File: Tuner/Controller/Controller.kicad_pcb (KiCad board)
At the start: 2 copper layers, 100 x 100 mm, 180 parts, among them J1 Conn_02x05_Odd_Even, J10 Conn_01x05, J11 Conn_Coaxial, J13 Conn_Coaxial, J15 Conn_01x02, J16 Conn_01x08, J18 Conn_01x01, J19 Conn_01x01, J2 Conn_02x05_Odd_Even, J20 Conn_01x01, J21 Conn_01x01, J3 Conn_02x05_Odd_Even, J4 Conn_02x05_Odd_Even, J5 Conn_02x05_Odd_Even, J6 Conn_01x02, J7 Conn_02x05_Odd_Even, J8 Conn_01x06, J9 Conn_Coaxial, Q1 2N3904, Q10 2N7000, Q11 2N7000, Q12 2N7000, Q2 2N3904, Q3 2N3904, Q4 2N3904, Q5 2N3904, Q6 2N3904, Q7 2N3904, Q8 2N3904, Q9 2N7000, U1 74LS393, U2 74HC14, U3 74HC86, U4 LM350_TO220

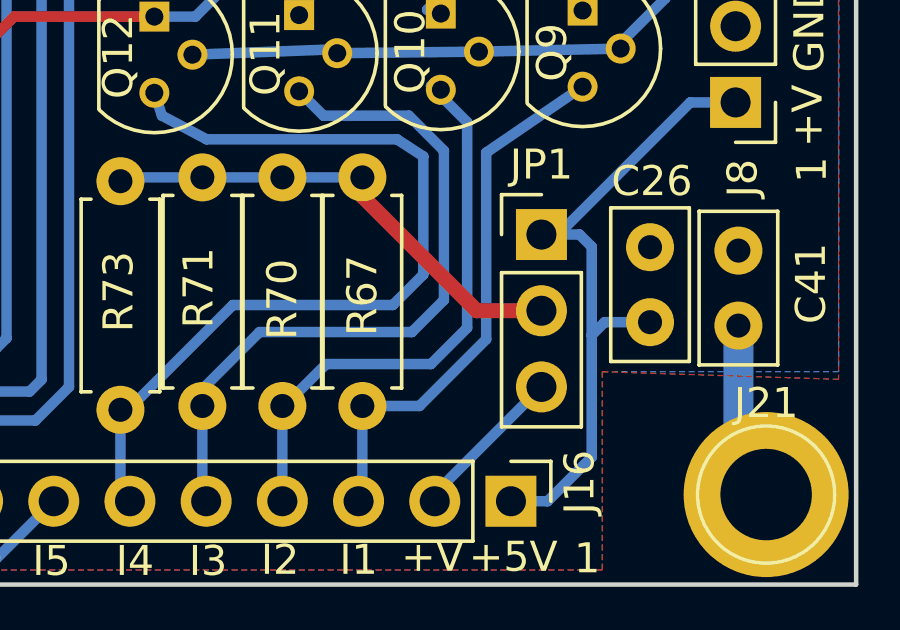
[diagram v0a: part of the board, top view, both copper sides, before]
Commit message: Added some initial I2C user interface stuff
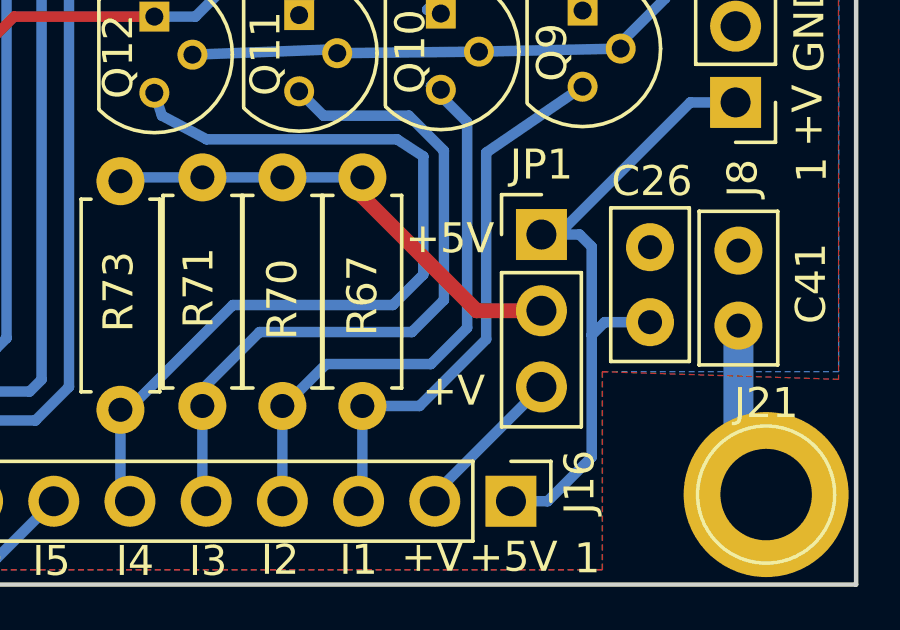
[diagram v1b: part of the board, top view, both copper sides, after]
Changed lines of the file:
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@@
     (links 401)
     (no_connects 0)
-    (area 52.252381 23.9975 155.74762 130.223619)
+    (area 53.924999 27.924999 154.075001 128.075001)
     (thickness 1.6)
-    (drawings 55)
+    (drawings 57)
     (tracks 1681)
     (zones 0)
@@
   )
   (setup
-    (last_trace_width 0.35)
+    (last_trace_width 0.25)
     (user_trace_width 0.35)
     (user_trace_width 0.5)
@@
     )
   )
+  (gr_text +5V (at 140.462 116.459) (layer F.SilkS)
+    (effects (font (size 1 1) (thickness 0.15)))
+  )
+  (gr_text +V (at 140.589 121.539) (layer F.SilkS)
+    (effects (font (size 1 1) (thickness 0.15)))
+  )
   (gr_text 1 (at 147.48764 41.95064 90) (layer F.SilkS)

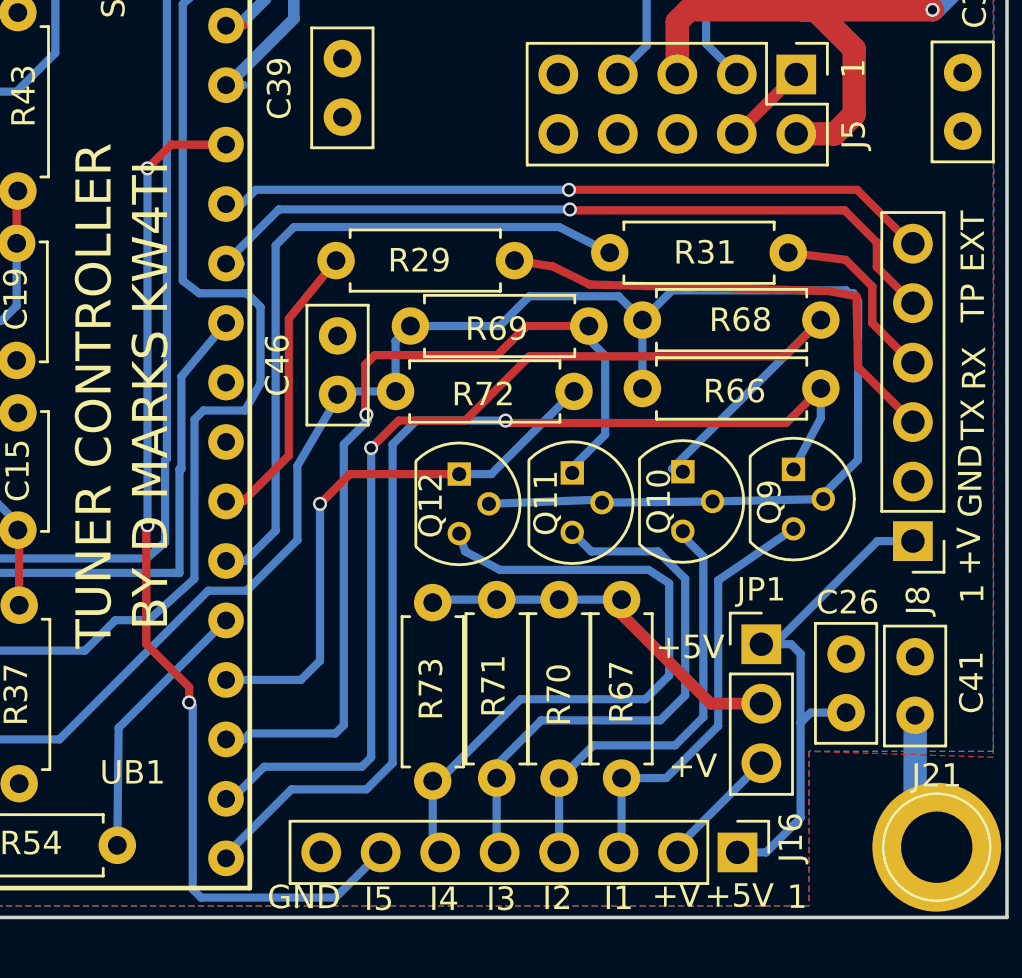
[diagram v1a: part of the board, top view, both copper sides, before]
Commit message: Moved digital signal interface connector over
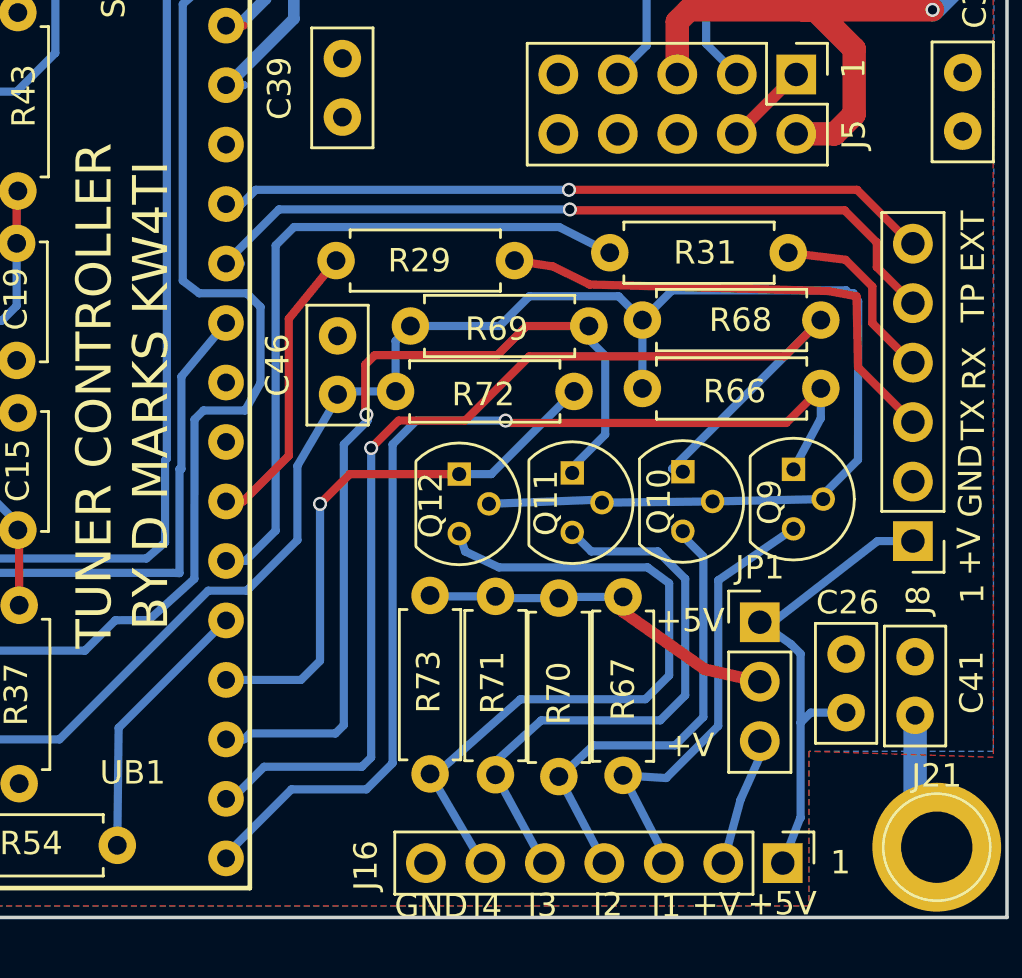
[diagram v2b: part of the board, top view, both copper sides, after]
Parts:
- J16: value Conn_01x08 -> Conn_01x07; footprint Pin_Headers:Pin_Header_Straight_1x08_Pitch2.54mm -> Pin_Headers:Pin_Header_Straight_1x07_Pitch2.54mm
- moved J16 1.98 mm to (144.4, 125.7)
- moved JP1 0.94 mm to (143.4, 115.4)
- moved R73 0.33 mm to (129.4, 121.9)
- moved R71 0.15 mm to (132.2, 121.9)
- moved R67 0.13 mm to (137.6, 121.9)
- moved R70 0.06 mm to (134.9, 122.0)
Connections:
- J16 pad 7: IO5 -> GND
- UB1 pad 41: IO5 -> (no net)
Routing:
- net IO5: track 44.4 -> 0.00 mm, vias 3 -> 0
- net +5V: track 134.2 -> 132.8 mm
- net Net-(J16-Pad6): track 29.0 -> 30.2 mm
- net Net-(J16-Pad5): track 24.3 -> 25.3 mm
- net Net-(J16-Pad4): track 19.6 -> 20.6 mm
- net Net-(J16-Pad3): track 18.6 -> 19.5 mm
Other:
- board text removed: "I5"
